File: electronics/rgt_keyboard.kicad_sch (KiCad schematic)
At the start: 34 parts, among them J10 Conn_01x04, J11 Conn_01x04, J12 Conn_01x04, J9 Conn_01x04, SW30 SW_SPST, SW31 SW_SPST, SW32 SW_SPST, SW33 SW_SPST, SW34 SW_SPST, SW35 SW_SPST, SW36 SW_SPST, SW37 SW_SPST, SW38 SW_SPST, SW39 SW_SPST, SW40 SW_SPST, SW41 SW_SPST, SW42 SW_SPST, SW43 SW_SPST, SW44 SW_SPST, SW45 SW_SPST, SW46 SW_SPST, SW47 SW_SPST, SW48 SW_SPST, SW49 SW_SPST, SW50 SW_SPST, SW51 SW_SPST, SW52 SW_SPST, SW53 SW_SPST, SW54 SW_SPST, SW55 SW_SPST, SW56 SW_SPST, SW57 SW_SPST, SW58 SW_SPST, U3 PCA9675PW

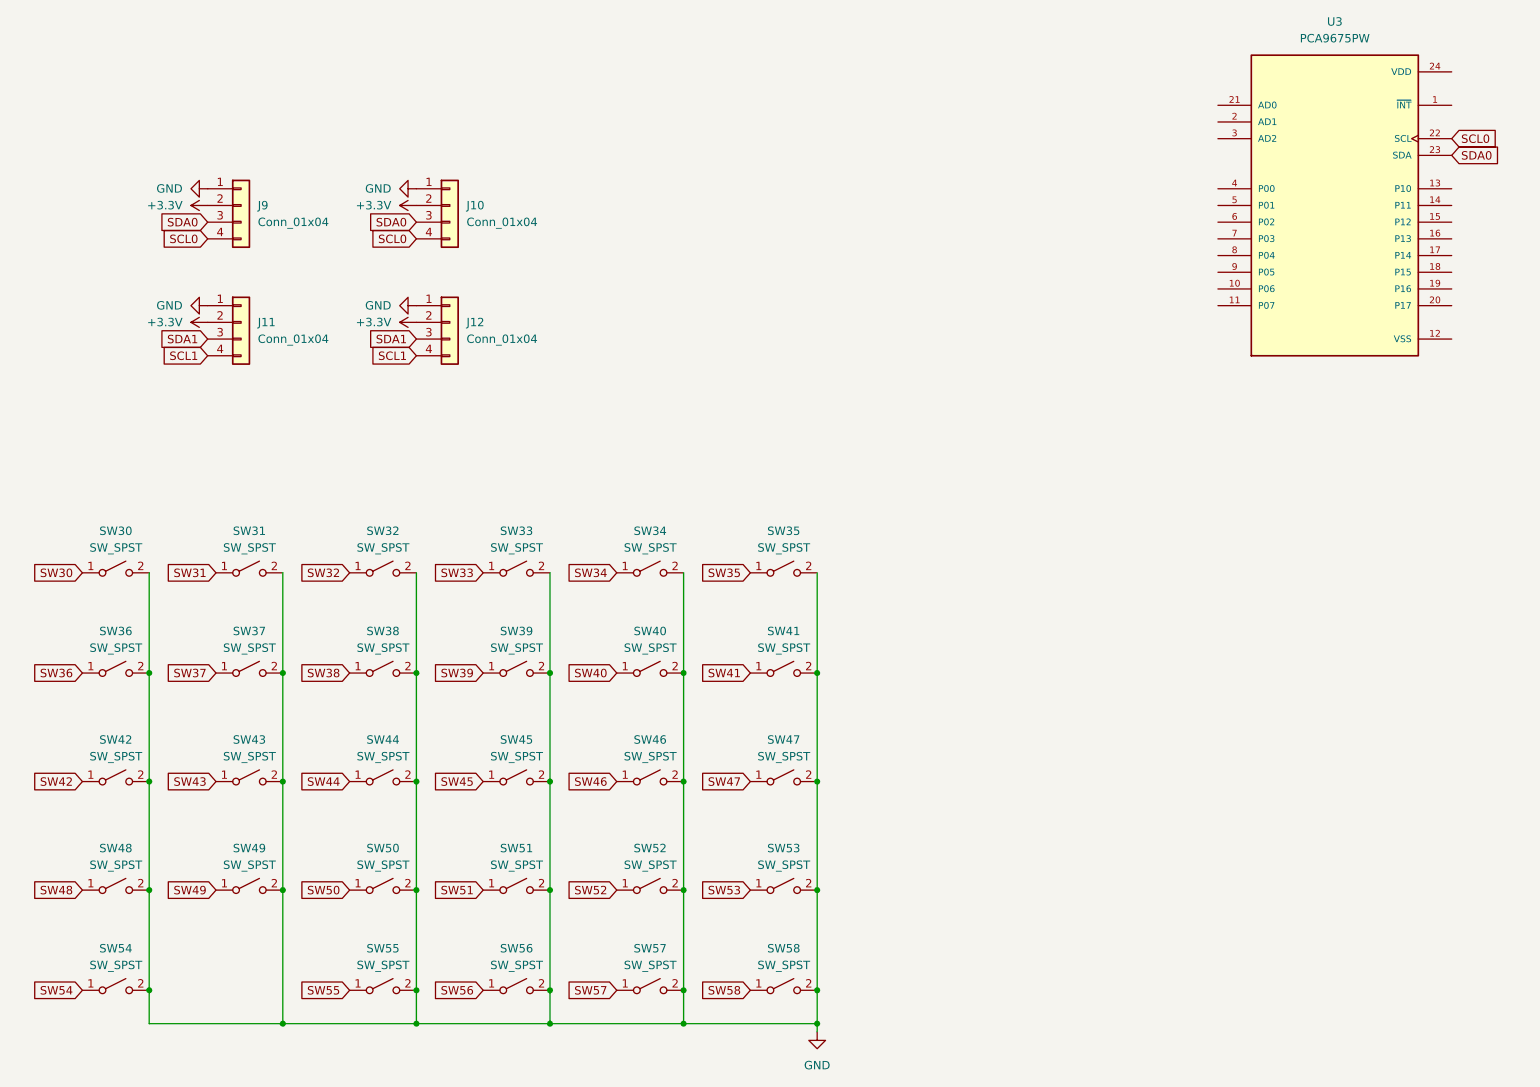
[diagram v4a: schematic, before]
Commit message: begin matrix via diodes
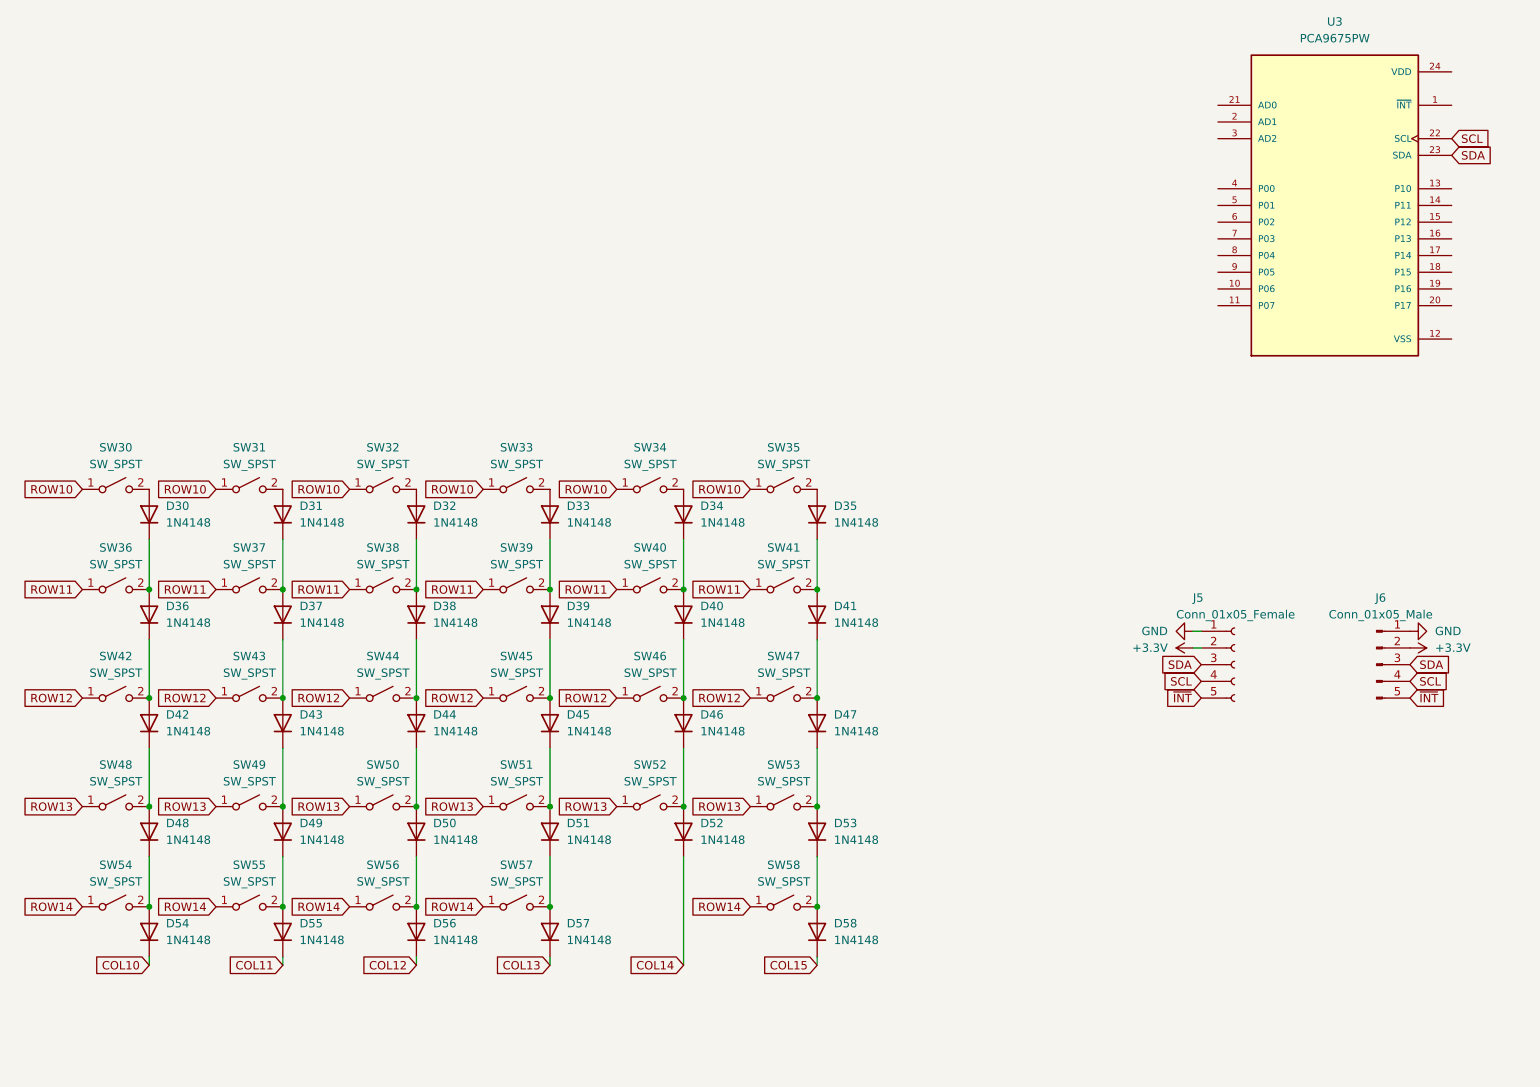
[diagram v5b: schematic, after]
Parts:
- removed J10, J11, J12, J9: Conn_01x04, symbol Connector_Generic:Conn_01x04
- added D30, D31, D32, D33, D34, D35, D36, D37, D38, D39, D40, D41, D42, D43, D44, D45, D46, D47, D48, D49, D50, D51, D52, D53, D54, D55, D56, D57, D58: 1N4148, Diode_SMD:D_SOD-123, symbol Diode:1N4148W
- added J5: Conn_01x05_Female, Connector_PinHeader_2.54mm:PinHeader_1x05_P2.54mm_Vertical, symbol Connector:Conn_01x05_Female
- added J6: Conn_01x05_Male, Connector_PinHeader_2.54mm:PinHeader_1x05_P2.54mm_Vertical, symbol Connector:Conn_01x05_Male
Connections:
- net SW31 is gone; now on net ROW10: SW31.1 (A)
- net SW32 is gone; now on net ROW10: SW32.1 (A)
- net SW33 is gone; now on net ROW10: SW33.1 (A)
- net SW34 is gone; now on net ROW10: SW34.1 (A)
- net SW35 is gone; now on net ROW10: SW35.1 (A)
- net SW37 is gone; now on net ROW11: SW37.1 (A)
- net SW38 is gone; now on net ROW11: SW38.1 (A)
- net SW39 is gone; now on net ROW11: SW39.1 (A)
- net SW40 is gone; now on net ROW11: SW40.1 (A)
- net SW41 is gone; now on net ROW11: SW41.1 (A)
- net SW43 is gone; now on net ROW12: SW43.1 (A)
- net SW44 is gone; now on net ROW12: SW44.1 (A)
- net SW45 is gone; now on net ROW12: SW45.1 (A)
- net SW46 is gone; now on net ROW12: SW46.1 (A)
- net SW47 is gone; now on net ROW12: SW47.1 (A)
- net SW49 is gone; now on net ROW13: SW49.1 (A)
- net SW50 is gone; now on net ROW13: SW50.1 (A)
- net SW51 is gone; now on net ROW13: SW51.1 (A)
- net SW52 is gone; now on net ROW13: SW52.1 (A)
- net SW53 is gone; now on net ROW13: SW53.1 (A)
- net SW55 is gone; now on net ROW14: SW55.1 (A)
- net SW56 is gone; now on net ROW14: SW56.1 (A)
- net SW57 is gone; now on net ROW14: SW57.1 (A)
- net SW58 is gone; now on net ROW14: SW58.1 (A)
- net +3V3: now also J5.2 (Pin_2), J6.2 (Pin_2)
- net GND: now also J5.1 (Pin_1), J6.1 (Pin_1); no longer SW30.2 (B), SW31.2 (B), SW32.2 (B), SW33.2 (B), SW34.2 (B), SW35.2 (B), SW36.2 (B), SW37.2 (B), SW38.2 (B), SW39.2 (B), SW40.2 (B), SW41.2 (B), SW42.2 (B), SW43.2 (B), SW44.2 (B), SW45.2 (B), SW46.2 (B), SW47.2 (B), SW48.2 (B), SW49.2 (B), SW50.2 (B), SW51.2 (B), SW52.2 (B), SW53.2 (B), SW54.2 (B), SW55.2 (B), SW56.2 (B), SW57.2 (B), SW58.2 (B)
- net SCL0 renamed SCL
- net SCL: now also J5.4 (Pin_4), J6.4 (Pin_4)
- net SDA0 renamed SDA
- net SDA: now also J5.3 (Pin_3), J6.3 (Pin_3)
- net SW30 renamed ROW10
- net SW36 renamed ROW11
- net SW42 renamed ROW12
- net SW48 renamed ROW13
- net SW54 renamed ROW14
- new net: D35.1 (K), D41.2 (A), SW41.2 (B)
- new net: D42.1 (K), D48.2 (A), SW48.2 (B)
- new net: D36.1 (K), D42.2 (A), SW42.2 (B)
- new net: D30.1 (K), D36.2 (A), SW36.2 (B)
- new net: D30.2 (A), SW30.2 (B)
- new net: D34.2 (A), SW34.2 (B)
- new net: D34.1 (K), D40.2 (A), SW40.2 (B)
- new net: D33.1 (K), D39.2 (A), SW39.2 (B)
- new net: D33.2 (A), SW33.2 (B)
- new net: D46.1 (K), D52.2 (A), SW52.2 (B)
- new net: D50.1 (K), D56.2 (A), SW56.2 (B)
- new net: D35.2 (A), SW35.2 (B)
- new net: D45.1 (K), D51.2 (A), SW51.2 (B)
- new net: D39.1 (K), D45.2 (A), SW45.2 (B)
- new net: D32.1 (K), D38.2 (A), SW38.2 (B)
- new net: D32.2 (A), SW32.2 (B)
- new net: D44.1 (K), D50.2 (A), SW50.2 (B)
- new net: D38.1 (K), D44.2 (A), SW44.2 (B)
- new net: D51.1 (K), D57.2 (A), SW57.2 (B)
- new net: D31.1 (K), D37.2 (A), SW37.2 (B)
- new net: D31.2 (A), SW31.2 (B)
- new net: D37.1 (K), D43.2 (A), SW43.2 (B)
- new net: D48.1 (K), D54.2 (A), SW54.2 (B)
- new net: D47.1 (K), D53.2 (A), SW53.2 (B)
- new net: D41.1 (K), D47.2 (A), SW47.2 (B)
- new net: D40.1 (K), D46.2 (A), SW46.2 (B)
- new net: D53.1 (K), D58.2 (A), SW58.2 (B)
- new net: D49.1 (K), D55.2 (A), SW55.2 (B)
- new net: D43.1 (K), D49.2 (A), SW49.2 (B)
- new net COL10: D54.1 (K)
- new net COL11: D55.1 (K)
- new net COL12: D56.1 (K)
- new net COL13: D57.1 (K)
- new net COL14: D52.1 (K)
- new net COL15: D58.1 (K)
- new net ~{INT}: J5.5 (Pin_5), J6.5 (Pin_5)

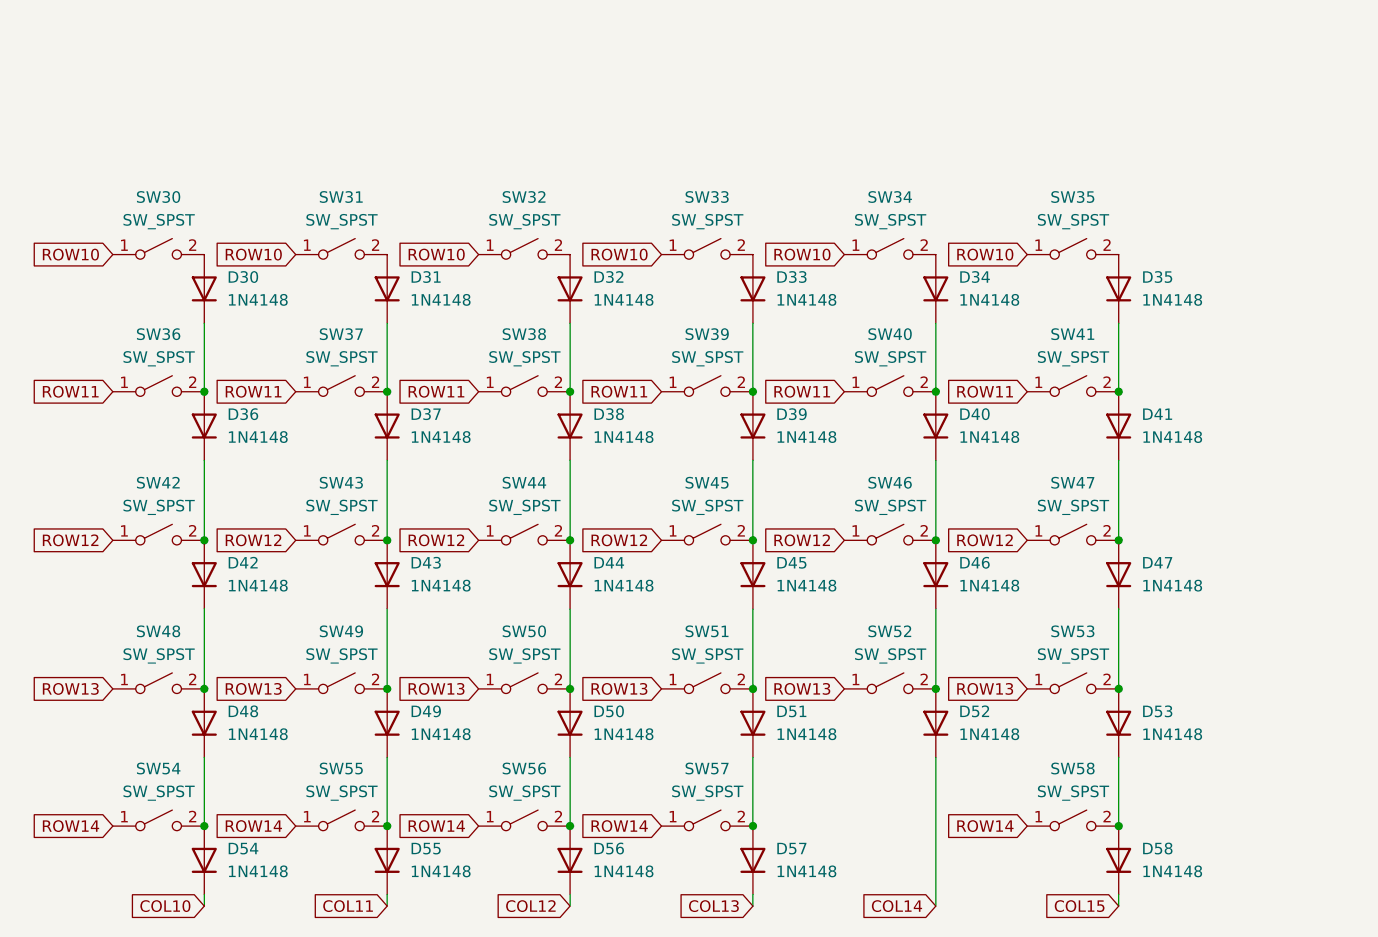
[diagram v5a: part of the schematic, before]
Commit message: reverse matrix diodes
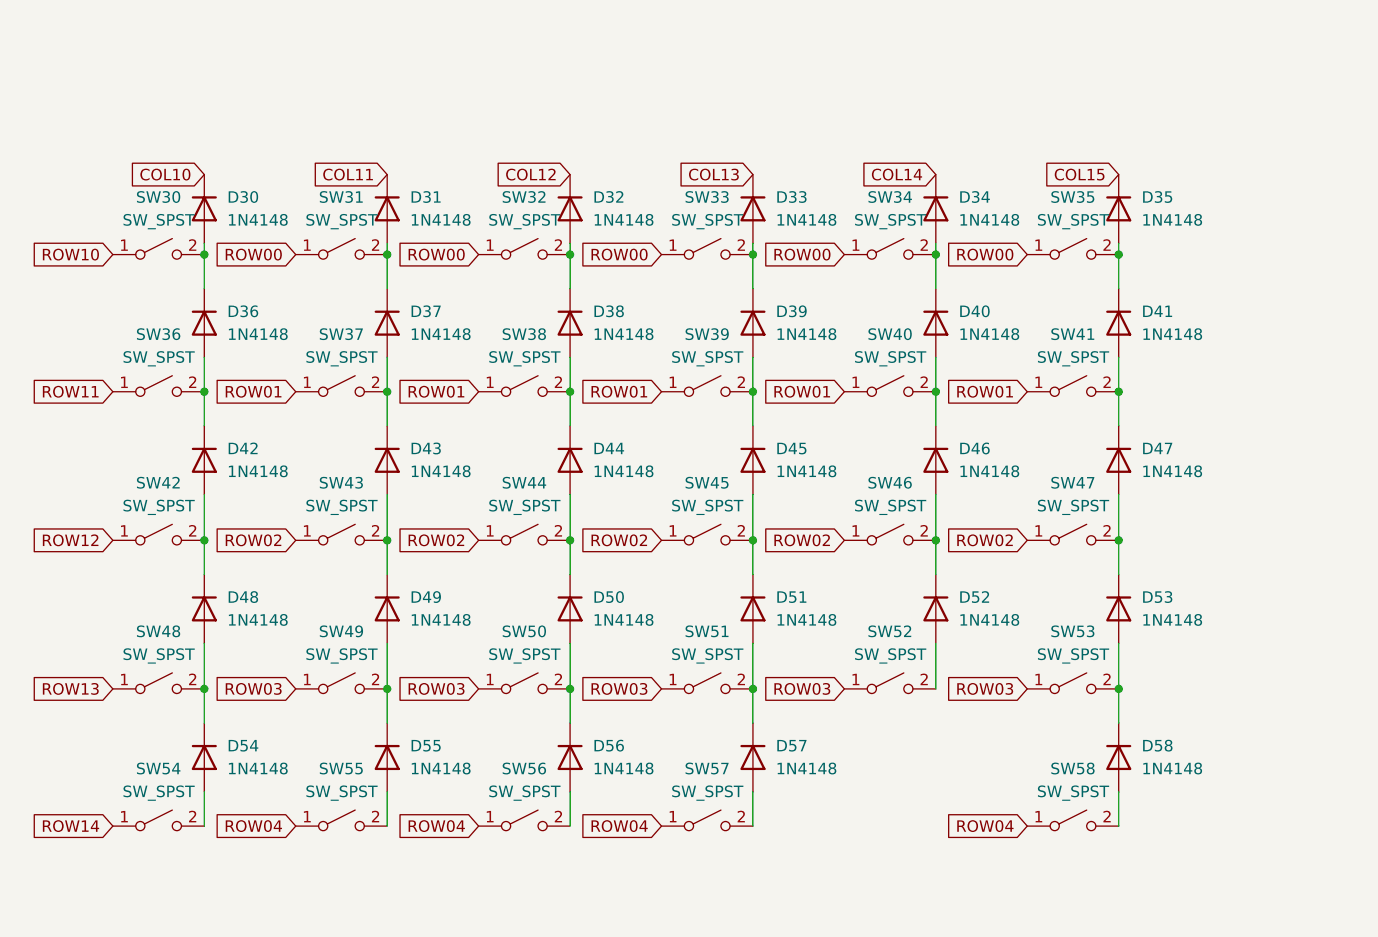
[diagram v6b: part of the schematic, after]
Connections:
- net COL10: now also D30.1 (K); no longer D54.1 (K)
- net COL11: now also D31.1 (K); no longer D55.1 (K)
- net COL12: now also D32.1 (K); no longer D56.1 (K)
- net COL13: now also D33.1 (K); no longer D57.1 (K)
- net COL14: now also D34.1 (K); no longer D52.1 (K)
- net COL15: now also D35.1 (K); no longer D58.1 (K)
- net ROW10: no longer SW31.1 (A), SW32.1 (A), SW33.1 (A), SW34.1 (A), SW35.1 (A)
- net ROW11: no longer SW37.1 (A), SW38.1 (A), SW39.1 (A), SW40.1 (A), SW41.1 (A)
- net ROW12: no longer SW43.1 (A), SW44.1 (A), SW45.1 (A), SW46.1 (A), SW47.1 (A)
- net ROW13: no longer SW49.1 (A), SW50.1 (A), SW51.1 (A), SW52.1 (A), SW53.1 (A)
- net ROW14: no longer SW55.1 (A), SW56.1 (A), SW57.1 (A), SW58.1 (A)
- net at D41.2 (A), SW41.2 (B): now also D47.1 (K); no longer D35.1 (K)
- net at D48.2 (A), SW48.2 (B): now also D54.1 (K); no longer D42.1 (K)
- net at D42.2 (A), SW42.2 (B): now also D48.1 (K); no longer D36.1 (K)
- net at D36.2 (A), SW36.2 (B): now also D42.1 (K); no longer D30.1 (K)
- net at D30.2 (A), SW30.2 (B): now also D36.1 (K)
- net at D34.2 (A), SW34.2 (B): now also D40.1 (K)
- net at D40.2 (A), SW40.2 (B): now also D46.1 (K); no longer D34.1 (K)
- net at D39.2 (A), SW39.2 (B): now also D45.1 (K); no longer D33.1 (K)
- net at D33.2 (A), SW33.2 (B): now also D39.1 (K)
- net at D52.2 (A), SW52.2 (B): no longer D46.1 (K)
- net at D56.2 (A), SW56.2 (B): no longer D50.1 (K)
- net at D35.2 (A), SW35.2 (B): now also D41.1 (K)
- net at D51.2 (A), SW51.2 (B): now also D57.1 (K); no longer D45.1 (K)
- net at D45.2 (A), SW45.2 (B): now also D51.1 (K); no longer D39.1 (K)
- net at D38.2 (A), SW38.2 (B): now also D44.1 (K); no longer D32.1 (K)
- net at D32.2 (A), SW32.2 (B): now also D38.1 (K)
- net at D50.2 (A), SW50.2 (B): now also D56.1 (K); no longer D44.1 (K)
- net at D44.2 (A), SW44.2 (B): now also D50.1 (K); no longer D38.1 (K)
- net at D57.2 (A), SW57.2 (B): no longer D51.1 (K)
- net at D37.2 (A), SW37.2 (B): now also D43.1 (K); no longer D31.1 (K)
- net at D31.2 (A), SW31.2 (B): now also D37.1 (K)
- net at D43.2 (A), SW43.2 (B): now also D49.1 (K); no longer D37.1 (K)
- net at D54.2 (A), SW54.2 (B): no longer D48.1 (K)
- net at D53.2 (A), SW53.2 (B): now also D58.1 (K); no longer D47.1 (K)
- net at D47.2 (A), SW47.2 (B): now also D53.1 (K); no longer D41.1 (K)
- net at D46.2 (A), SW46.2 (B): now also D52.1 (K); no longer D40.1 (K)
- net at D58.2 (A), SW58.2 (B): no longer D53.1 (K)
- net at D55.2 (A), SW55.2 (B): no longer D49.1 (K)
- net at D49.2 (A), SW49.2 (B): now also D55.1 (K); no longer D43.1 (K)
- new net ROW00: SW31.1 (A), SW32.1 (A), SW33.1 (A), SW34.1 (A), SW35.1 (A)
- new net ROW01: SW37.1 (A), SW38.1 (A), SW39.1 (A), SW40.1 (A), SW41.1 (A)
- new net ROW02: SW43.1 (A), SW44.1 (A), SW45.1 (A), SW46.1 (A), SW47.1 (A)
- new net ROW03: SW49.1 (A), SW50.1 (A), SW51.1 (A), SW52.1 (A), SW53.1 (A)
- new net ROW04: SW55.1 (A), SW56.1 (A), SW57.1 (A), SW58.1 (A)

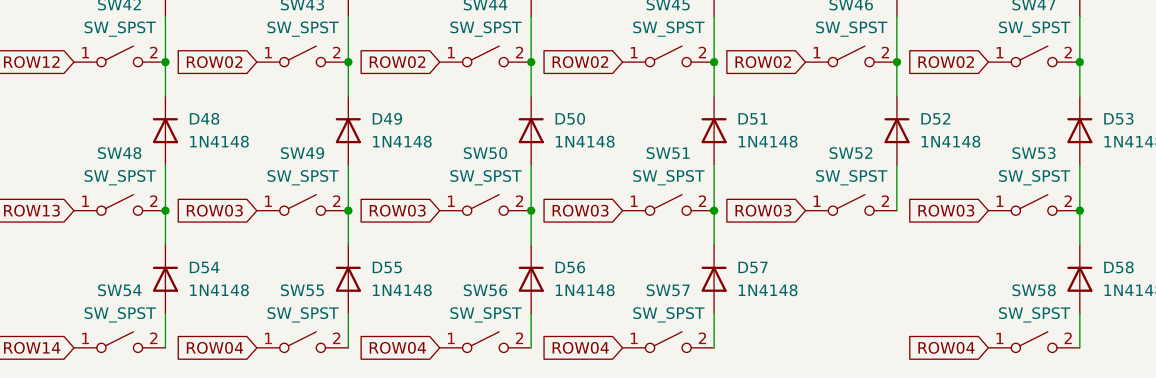
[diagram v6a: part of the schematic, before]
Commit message: fix right keyboard matrix
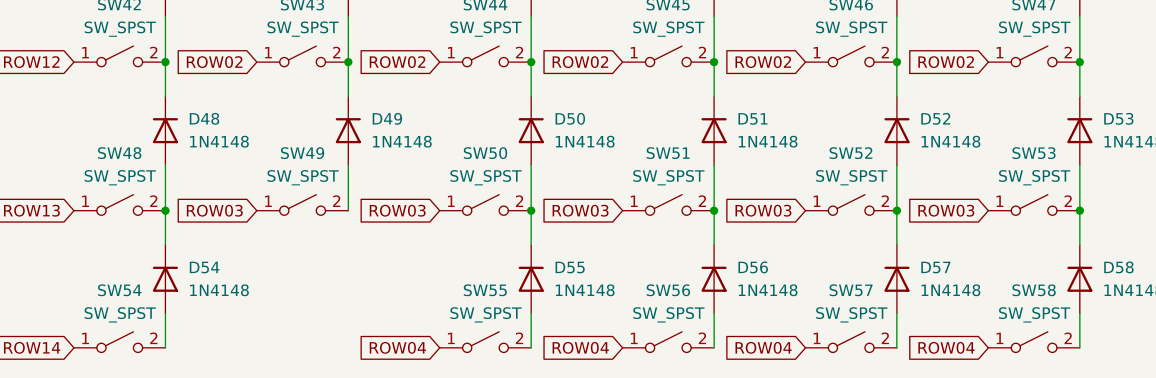
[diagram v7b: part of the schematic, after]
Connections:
- net at D51.2 (A), SW51.2 (B): now also D56.1 (K); no longer D57.1 (K)
- net at D50.2 (A), SW50.2 (B): now also D55.1 (K); no longer D56.1 (K)
- net at D49.2 (A), SW49.2 (B): no longer D55.1 (K)
- net at D52.2 (A), SW52.2 (B): now also D57.1 (K)
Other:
- moved on the sheet: D55, D56, D57, SW55, SW56, SW57
